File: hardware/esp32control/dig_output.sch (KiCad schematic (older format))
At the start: 6 parts, among them Q1 BSS138, U2 AQY212

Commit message: pcb update
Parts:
- R1: value 10k -> 1k
- R2: value 470 -> 1k
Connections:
- net VDD: now also U2.1; no longer R1.2
- net nIn: no longer U2.2
- net at R1.1: now also Q1.3 (D), R2.2; no longer U2.1
- net at D1.1 (K): now also R2.1; no longer R2.2
- new net: R1.2, U2.2
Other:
- moved on the sheet: D11, Q4, R26, R27
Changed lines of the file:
@@
 $Descr A4 11693 8268
 encoding utf-8
-Sheet 2 5
+Sheet 5 5
 Title ""
 Date ""
@@
 AR Path="/5C1F9DEA/5C1D222E" Ref="U6"  Part="1"
 AR Path="/5C1F9DF5/5C1D222E" Ref="U7"  Part="1"
-F 0 "U2" H 5300 3215 50  0000 C CNN
+F 0 "U7" H 5300 3215 50  0000 C CNN
 F 1 "AQY212" H 5300 3124 50  0000 C CNN
 F 2 "Housings_DIP:DIP-4_W7.62mm_SMDSocket_SmallPads" H 5300 3033 50  0000 C CIN
@@
 	1    0    0    -1
 $EndComp
-Wire Wire Line
-	5000 2900 4250 2900
 Text Label 4650 2900 0    60   ~ 0
 CH1
@@
 L esp32control-rescue:R-device-esp32ValveControl-rescue R1
 U 1 1 5C1D2239
-P 4850 2700
+P 4750 3350
 AR Path="/5C171864/5C1D2239" Ref="R1"  Part="1"
 AR Path="/5C171864/5C1D0CB5/5C1D2239" Ref="R?"  Part="1"
@@
 AR Path="/5C1F9DF5/5C1D2239" Ref="R26"  Part="1"
 AR Path="/5C1D2239" Ref="R26"  Part="1"
-F 0 "R1" V 4930 2700 50  0000 C CNN
-F 1 "10k" V 4850 2700 50  0000 C CNN
-F 2 "Resistors_SMD:R_0603" V 4780 2700 30  0001 C CNN
-F 3 "" H 4850 2700 30  0000 C CNN
-	1    4850 2700
-	0    1    -1   0
+F 0 "R26" V 4830 3350 50  0000 C CNN
+F 1 "1k" V 4750 3350 50  0000 C CNN
+F 2 "Resistors_SMD:R_0603" V 4680 3350 30  0001 C CNN
+F 3 "" H 4750 3350 30  0000 C CNN
+	1    4750 3350
+	1    0    0    1
 $EndComp
 Text HLabel 4150 2900 0    60   Input ~ 0
@@
 Text HLabel 6200 2900 2    60   Output ~ 0
 Out
-Wire Wire Line
-	4700 2700 4350 2700
 Text HLabel 6000 2700 2    60   Input ~ 0
 Vin
@@
 AR Path="/5C1F9DEA/5C1D2245" Ref="D10"  Part="1"
 AR Path="/5C1F9DF5/5C1D2245" Ref="D12"  Part="1"
-F 0 "D2" H 6000 3350 50  0000 C CNN
+F 0 "D12" H 6000 3350 50  0000 C CNN
 F 1 "TVS" H 6000 3050 50  0000 C CNN
 F 2 "Diodes_SMD:D_SMA" H 6000 3200 60  0001 C CNN
@@
 Wire Wire Line
 	6000 2900 6200 2900
-Text HLabel 6200 3800 2    60   Input ~ 0
+Text HLabel 6200 3900 2    60   Input ~ 0
 GND
 $Comp
 L esp32control-rescue:LED-device-esp32ValveControl-rescue D?
 U 1 1 5C1D2251
-P 4750 3500
+P 4500 2950
 AR Path="/5C1D2251" Ref="D?"  Part="1"
 AR Path="/5C171864/5C1D2251" Ref="D1"  Part="1"
@@
 AR Path="/5C1F9DEA/5C1D2251" Ref="D9"  Part="1"
 AR Path="/5C1F9DF5/5C1D2251" Ref="D11"  Part="1"
-F 0 "D1" H 4750 3600 50  0000 C CNN
-F 1 "LED" H 4750 3400 50  0000 C CNN
-F 2 "LEDs:LED_0603_HandSoldering" H 4750 3500 50  0001 C CNN
-F 3 "" H 4750 3500 50  0000 C CNN
-	1    4750 3500
-	-1   0    0    1
-$EndComp
-$Comp
-L transistors:BSS138 Q?
-U 1 1 5C1D2258
-P 5450 3600
-AR Path="/5C1D2258" Ref="Q?"  Part="1"
-AR Path="/5C171864/5C1D2258" Ref="Q1"  Part="1"
-AR Path="/5C1F3716/5C1D2258" Ref="Q2"  Part="1"
-AR Path="/5C1F9DEA/5C1D2258" Ref="Q3"  Part="1"
-AR Path="/5C1F9DF5/5C1D2258" Ref="Q4"  Part="1"
-F 0 "Q1" H 5450 3451 40  0000 R CNN
-F 1 "BSS138" H 5450 3750 40  0000 R CNN
-F 2 "Package_TO_SOT_SMD:SOT-23" H 5320 3702 29  0000 C CNN
-F 3 "" H 5450 3600 60  0000 C CNN
-	1    5450 3600
+F 0 "D11" H 4500 3050 50  0000 C CNN
+F 1 "LED" H 4500 2850 50  0000 C CNN
+F 2 "LEDs:LED_0603_HandSoldering" H 4500 2950 50  0001 C CNN
+F 3 "" H 4500 2950 50  0000 C CNN
+	1    4500 2950
 	0    -1   -1   0
 $EndComp
@@
 L esp32control-rescue:R-device-esp32ValveControl-rescue R?
 U 1 1 5C1D225F
-P 5100 3500
+P 4500 3350
 AR Path="/5C1D225F" Ref="R?"  Part="1"
 AR Path="/5C171864/5C1D225F" Ref="R2"  Part="1"
@@
 AR Path="/5C1F9DEA/5C1D225F" Ref="R25"  Part="1"
 AR Path="/5C1F9DF5/5C1D225F" Ref="R27"  Part="1"
-F 0 "R2" V 5180 3500 50  0000 C CNN
-F 1 "470" V 5100 3500 50  0000 C CNN
-F 2 "Resistors_SMD:R_0603" V 5030 3500 30  0001 C CNN
-F 3 "" H 5100 3500 30  0000 C CNN
-	1    5100 3500
-	0    1    1    0
+F 0 "R27" V 4580 3350 50  0000 C CNN
+F 1 "1k" V 4500 3350 50  0000 C CNN
+F 2 "Resistors_SMD:R_0603" V 4430 3350 30  0001 C CNN
+F 3 "" H 4500 3350 30  0000 C CNN
+	1    4500 3350
+	1    0    0    -1
 $EndComp
 Wire Wire Line
-	4550 3500 4350 3500
-Wire Wire Line
-	4350 3500 4350 2700
-Connection ~ 4350 2700
-Wire Wire Line
-	4350 2700 4150 2700
-Wire Wire Line
-	5500 3800 4250 3800
-Wire Wire Line
-	4250 3800 4250 2900
-Connection ~ 4250 2900
+	4250 3750 4250 2900
 Wire Wire Line
 	4250 2900 4150 2900
-Wire Wire Line
-	5650 3800 5650 3500
 Text HLabel 6200 3550 2    50   Input ~ 0
 GNDA
@@
 	6000 3550 6000 3500
 Wire Wire Line
-	5650 3800 6200 3800
+	4300 3750 4250 3750
+$Comp
+L transistors:BSS138 Q?
+U 1 1 5C1D2258
+P 4500 3700
+AR Path="/5C1D2258" Ref="Q?"  Part="1"
+AR Path="/5C171864/5C1D2258" Ref="Q1"  Part="1"
+AR Path="/5C1F3716/5C1D2258" Ref="Q2"  Part="1"
+AR Path="/5C1F9DEA/5C1D2258" Ref="Q3"  Part="1"
+AR Path="/5C1F9DF5/5C1D2258" Ref="Q4"  Part="1"
+F 0 "Q4" H 4500 3551 40  0000 R CNN
+F 1 "BSS138" H 4500 3850 40  0000 R CNN
+F 2 "Package_TO_SOT_SMD:SOT-23" H 4370 3802 29  0000 C CNN
+F 3 "" H 4500 3700 60  0000 C CNN
+	1    4500 3700
+	1    0    0    -1
+$EndComp
+Wire Wire Line
+	5000 2900 4750 2900
+Wire Wire Line
+	4150 2700 4500 2700
+Wire Wire Line
+	4500 2750 4500 2700
+Connection ~ 4500 2700
+Wire Wire Line
+	4500 3150 4500 3200
+Wire Wire Line
+	4500 3500 4600 3500
+Wire Wire Line
+	4750 3200 4750 2900
+Wire Wire Line
+	4500 2700 5000 2700
+Connection ~ 4600 3500
+Wire Wire Line
+	4600 3500 4750 3500
+Wire Wire Line
+	4600 3900 6200 3900
 $EndSCHEMATC

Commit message: update libs to kicad 5.1.5
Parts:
- D2: footprint Diodes_SMD:D_SMA -> Diode_SMD:D_SMA
- R1, R2: footprint Resistors_SMD:R_0603 -> Resistor_SMD:R_0603_1608Metric; symbol esp32control-rescue:R-device-esp32ValveControl-rescue -> Device:R
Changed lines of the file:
@@
 EESchema Schematic File Version 4
-LIBS:esp32control-cache
-EELAYER 26 0
+EELAYER 30 0
 EELAYER END
 $Descr A4 11693 8268
 encoding utf-8
-Sheet 5 5
+Sheet 2 5
 Title ""
 Date ""
@@
 AR Path="/5C1F9DEA/5C1D222E" Ref="U6"  Part="1"
 AR Path="/5C1F9DF5/5C1D222E" Ref="U7"  Part="1"
-F 0 "U7" H 5300 3215 50  0000 C CNN
+F 0 "U2" H 5300 3215 50  0000 C CNN
 F 1 "AQY212" H 5300 3124 50  0000 C CNN
 F 2 "Housings_DIP:DIP-4_W7.62mm_SMDSocket_SmallPads" H 5300 3033 50  0000 C CIN
@@
 Vin
 $Comp
-L esp32control-rescue:R-device-esp32ValveControl-rescue R1
+L Device:R R1
 U 1 1 5C1D2239
 P 4750 3350
@@
 AR Path="/5C1F9DF5/5C1D2239" Ref="R26"  Part="1"
 AR Path="/5C1D2239" Ref="R26"  Part="1"
-F 0 "R26" V 4830 3350 50  0000 C CNN
+F 0 "R1" V 4830 3350 50  0000 C CNN
 F 1 "1k" V 4750 3350 50  0000 C CNN
-F 2 "Resistors_SMD:R_0603" V 4680 3350 30  0001 C CNN
+F 2 "Resistor_SMD:R_0603_1608Metric" V 4680 3350 30  0001 C CNN
 F 3 "" H 4750 3350 30  0000 C CNN
 	1    4750 3350
@@
 AR Path="/5C1F9DEA/5C1D2245" Ref="D10"  Part="1"
 AR Path="/5C1F9DF5/5C1D2245" Ref="D12"  Part="1"
-F 0 "D12" H 6000 3350 50  0000 C CNN
+F 0 "D2" H 6000 3350 50  0000 C CNN
 F 1 "TVS" H 6000 3050 50  0000 C CNN
-F 2 "Diodes_SMD:D_SMA" H 6000 3200 60  0001 C CNN
+F 2 "Diode_SMD:D_SMA" H 6000 3200 60  0001 C CNN
 F 3 "" H 6000 3200 60  0000 C CNN
 	1    6000 3200
@@
 AR Path="/5C1F9DEA/5C1D2251" Ref="D9"  Part="1"
 AR Path="/5C1F9DF5/5C1D2251" Ref="D11"  Part="1"
-F 0 "D11" H 4500 3050 50  0000 C CNN
+F 0 "D1" H 4500 3050 50  0000 C CNN
 F 1 "LED" H 4500 2850 50  0000 C CNN
 F 2 "LEDs:LED_0603_HandSoldering" H 4500 2950 50  0001 C CNN
@@
 $EndComp
 $Comp
-L esp32control-rescue:R-device-esp32ValveControl-rescue R?
+L Device:R R?
 U 1 1 5C1D225F
 P 4500 3350
@@
 AR Path="/5C1F9DEA/5C1D225F" Ref="R25"  Part="1"
 AR Path="/5C1F9DF5/5C1D225F" Ref="R27"  Part="1"
-F 0 "R27" V 4580 3350 50  0000 C CNN
+F 0 "R2" V 4580 3350 50  0000 C CNN
 F 1 "1k" V 4500 3350 50  0000 C CNN
-F 2 "Resistors_SMD:R_0603" V 4430 3350 30  0001 C CNN
+F 2 "Resistor_SMD:R_0603_1608Metric" V 4430 3350 30  0001 C CNN
 F 3 "" H 4500 3350 30  0000 C CNN
 	1    4500 3350
@@
 AR Path="/5C1F9DEA/5C1D2258" Ref="Q3"  Part="1"
 AR Path="/5C1F9DF5/5C1D2258" Ref="Q4"  Part="1"
-F 0 "Q4" H 4500 3551 40  0000 R CNN
+F 0 "Q1" H 4500 3551 40  0000 R CNN
 F 1 "BSS138" H 4500 3850 40  0000 R CNN
 F 2 "Package_TO_SOT_SMD:SOT-23" H 4370 3802 29  0000 C CNN

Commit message: revB initial
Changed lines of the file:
@@
 AR Path="/5C1F9DEA/5C1D222E" Ref="U6"  Part="1"
 AR Path="/5C1F9DF5/5C1D222E" Ref="U7"  Part="1"
-F 0 "U2" H 5300 3215 50  0000 C CNN
+F 0 "U7" H 5300 3215 50  0000 C CNN
 F 1 "AQY212" H 5300 3124 50  0000 C CNN
 F 2 "Housings_DIP:DIP-4_W7.62mm_SMDSocket_SmallPads" H 5300 3033 50  0000 C CIN
@@
 AR Path="/5C1F9DF5/5C1D2239" Ref="R26"  Part="1"
 AR Path="/5C1D2239" Ref="R26"  Part="1"
-F 0 "R1" V 4830 3350 50  0000 C CNN
+F 0 "R26" V 4830 3350 50  0000 C CNN
 F 1 "1k" V 4750 3350 50  0000 C CNN
 F 2 "Resistor_SMD:R_0603_1608Metric" V 4680 3350 30  0001 C CNN
@@
 AR Path="/5C1F9DEA/5C1D2245" Ref="D10"  Part="1"
 AR Path="/5C1F9DF5/5C1D2245" Ref="D12"  Part="1"
-F 0 "D2" H 6000 3350 50  0000 C CNN
+F 0 "D12" H 6000 3350 50  0000 C CNN
 F 1 "TVS" H 6000 3050 50  0000 C CNN
 F 2 "Diode_SMD:D_SMA" H 6000 3200 60  0001 C CNN
@@
 AR Path="/5C1F9DEA/5C1D2251" Ref="D9"  Part="1"
 AR Path="/5C1F9DF5/5C1D2251" Ref="D11"  Part="1"
-F 0 "D1" H 4500 3050 50  0000 C CNN
+F 0 "D11" H 4500 3050 50  0000 C CNN
 F 1 "LED" H 4500 2850 50  0000 C CNN
 F 2 "LEDs:LED_0603_HandSoldering" H 4500 2950 50  0001 C CNN
@@
 AR Path="/5C1F9DEA/5C1D225F" Ref="R25"  Part="1"
 AR Path="/5C1F9DF5/5C1D225F" Ref="R27"  Part="1"
-F 0 "R2" V 4580 3350 50  0000 C CNN
+F 0 "R27" V 4580 3350 50  0000 C CNN
 F 1 "1k" V 4500 3350 50  0000 C CNN
 F 2 "Resistor_SMD:R_0603_1608Metric" V 4430 3350 30  0001 C CNN
@@
 AR Path="/5C1F9DEA/5C1D2258" Ref="Q3"  Part="1"
 AR Path="/5C1F9DF5/5C1D2258" Ref="Q4"  Part="1"
-F 0 "Q1" H 4500 3551 40  0000 R CNN
+F 0 "Q4" H 4500 3551 40  0000 R CNN
 F 1 "BSS138" H 4500 3850 40  0000 R CNN
 F 2 "Package_TO_SOT_SMD:SOT-23" H 4370 3802 29  0000 C CNN

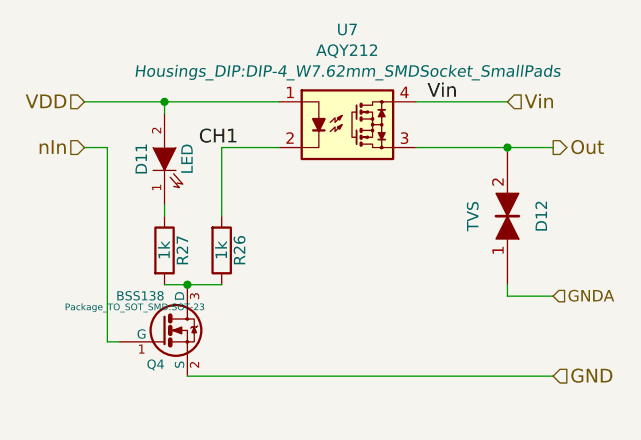
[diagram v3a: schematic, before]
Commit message: switched position of con and esp in layout
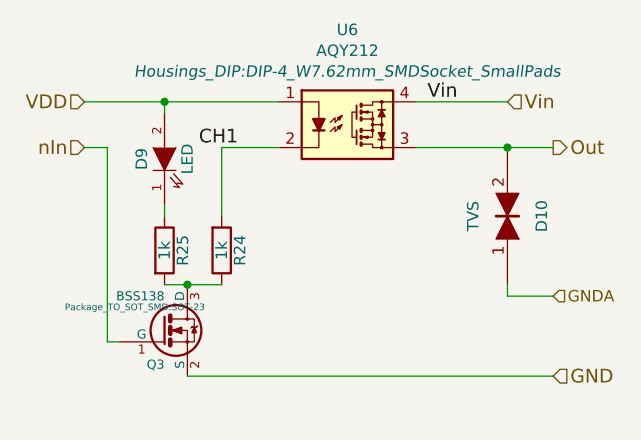
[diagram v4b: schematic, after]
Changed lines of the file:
@@
 $Descr A4 11693 8268
 encoding utf-8
-Sheet 2 5
+Sheet 4 5
 Title ""
 Date ""
@@
 AR Path="/5C1F9DEA/5C1D222E" Ref="U6"  Part="1"
 AR Path="/5C1F9DF5/5C1D222E" Ref="U7"  Part="1"
-F 0 "U7" H 5300 3215 50  0000 C CNN
+F 0 "U6" H 5300 3215 50  0000 C CNN
 F 1 "AQY212" H 5300 3124 50  0000 C CNN
 F 2 "Housings_DIP:DIP-4_W7.62mm_SMDSocket_SmallPads" H 5300 3033 50  0000 C CIN
@@
 AR Path="/5C1F9DF5/5C1D2239" Ref="R26"  Part="1"
 AR Path="/5C1D2239" Ref="R26"  Part="1"
-F 0 "R26" V 4830 3350 50  0000 C CNN
+F 0 "R24" V 4830 3350 50  0000 C CNN
 F 1 "1k" V 4750 3350 50  0000 C CNN
 F 2 "Resistor_SMD:R_0603_1608Metric" V 4680 3350 30  0001 C CNN
@@
 AR Path="/5C1F9DEA/5C1D2245" Ref="D10"  Part="1"
 AR Path="/5C1F9DF5/5C1D2245" Ref="D12"  Part="1"
-F 0 "D12" H 6000 3350 50  0000 C CNN
+F 0 "D10" H 6000 3350 50  0000 C CNN
 F 1 "TVS" H 6000 3050 50  0000 C CNN
 F 2 "Diode_SMD:D_SMA" H 6000 3200 60  0001 C CNN
@@
 AR Path="/5C1F9DEA/5C1D2251" Ref="D9"  Part="1"
 AR Path="/5C1F9DF5/5C1D2251" Ref="D11"  Part="1"
-F 0 "D11" H 4500 3050 50  0000 C CNN
+F 0 "D9" H 4500 3050 50  0000 C CNN
 F 1 "LED" H 4500 2850 50  0000 C CNN
 F 2 "LEDs:LED_0603_HandSoldering" H 4500 2950 50  0001 C CNN
@@
 AR Path="/5C1F9DEA/5C1D225F" Ref="R25"  Part="1"
 AR Path="/5C1F9DF5/5C1D225F" Ref="R27"  Part="1"
-F 0 "R27" V 4580 3350 50  0000 C CNN
+F 0 "R25" V 4580 3350 50  0000 C CNN
 F 1 "1k" V 4500 3350 50  0000 C CNN
 F 2 "Resistor_SMD:R_0603_1608Metric" V 4430 3350 30  0001 C CNN
@@
 AR Path="/5C1F9DEA/5C1D2258" Ref="Q3"  Part="1"
 AR Path="/5C1F9DF5/5C1D2258" Ref="Q4"  Part="1"
-F 0 "Q4" H 4500 3551 40  0000 R CNN
+F 0 "Q3" H 4500 3551 40  0000 R CNN
 F 1 "BSS138" H 4500 3850 40  0000 R CNN
 F 2 "Package_TO_SOT_SMD:SOT-23" H 4370 3802 29  0000 C CNN

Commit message: bom update
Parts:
- D2: value TVS -> SMAJ26CAQ; Mouser (none) -> 621-SMAJ26CAQ-13-F
- Q1: Mouser (none) -> 771-BSS138P215
- U2: Mouser (none) -> 769-AQY212GS
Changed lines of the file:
@@
 F 2 "Housings_DIP:DIP-4_W7.62mm_SMDSocket_SmallPads" H 5300 3033 50  0000 C CIN
 F 3 "http://www.semicon.toshiba.co.jp/docs/datasheet/en/Opto/TLP222A_TLP222A-2_en_datasheet_071001.pdf" H 5300 3034 50  0001 C CNN
+F 4 " 769-AQY212GS " H 5300 2800 50  0001 C CNN "Mouser"
 	1    5300 2800
 	1    0    0    -1
@@
 AR Path="/5C1F9DF5/5C1D2245" Ref="D12"  Part="1"
 F 0 "D10" H 6000 3350 50  0000 C CNN
-F 1 "TVS" H 6000 3050 50  0000 C CNN
+F 1 "SMAJ26CAQ" H 6000 3050 50  0000 C CNN
 F 2 "Diode_SMD:D_SMA" H 6000 3200 60  0001 C CNN
 F 3 "" H 6000 3200 60  0000 C CNN
+F 4 " 621-SMAJ26CAQ-13-F " H 6000 3200 50  0001 C CNN "Mouser"
 	1    6000 3200
 	0    1    -1   0
@@
 F 2 "Package_TO_SOT_SMD:SOT-23" H 4370 3802 29  0000 C CNN
 F 3 "" H 4500 3700 60  0000 C CNN
+F 4 " 771-BSS138P215 " H 4500 3700 50  0001 C CNN "Mouser"
 	1    4500 3700
 	1    0    0    -1

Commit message: kicad6 update
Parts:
- D1: value LED -> yellow; Mouser (none) -> 710-150060YS75000
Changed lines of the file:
@@
 $Descr A4 11693 8268
 encoding utf-8
-Sheet 4 5
+Sheet 2 5
 Title ""
 Date ""
@@
 AR Path="/5C1F9DEA/5C1D222E" Ref="U6"  Part="1"
 AR Path="/5C1F9DF5/5C1D222E" Ref="U7"  Part="1"
-F 0 "U6" H 5300 3215 50  0000 C CNN
+F 0 "U2" H 5300 3215 50  0000 C CNN
 F 1 "AQY212" H 5300 3124 50  0000 C CNN
 F 2 "Housings_DIP:DIP-4_W7.62mm_SMDSocket_SmallPads" H 5300 3033 50  0000 C CIN
@@
 AR Path="/5C1F9DF5/5C1D2239" Ref="R26"  Part="1"
 AR Path="/5C1D2239" Ref="R26"  Part="1"
-F 0 "R24" V 4830 3350 50  0000 C CNN
+F 0 "R1" V 4830 3350 50  0000 C CNN
 F 1 "1k" V 4750 3350 50  0000 C CNN
 F 2 "Resistor_SMD:R_0603_1608Metric" V 4680 3350 30  0001 C CNN
@@
 AR Path="/5C1F9DEA/5C1D2245" Ref="D10"  Part="1"
 AR Path="/5C1F9DF5/5C1D2245" Ref="D12"  Part="1"
-F 0 "D10" H 6000 3350 50  0000 C CNN
+F 0 "D2" H 6000 3350 50  0000 C CNN
 F 1 "SMAJ26CAQ" H 6000 3050 50  0000 C CNN
 F 2 "Diode_SMD:D_SMA" H 6000 3200 60  0001 C CNN
@@
 AR Path="/5C1F9DEA/5C1D2251" Ref="D9"  Part="1"
 AR Path="/5C1F9DF5/5C1D2251" Ref="D11"  Part="1"
-F 0 "D9" H 4500 3050 50  0000 C CNN
-F 1 "LED" H 4500 2850 50  0000 C CNN
+F 0 "D1" H 4500 3050 50  0000 C CNN
+F 1 "yellow" H 4500 2850 50  0000 C CNN
 F 2 "LEDs:LED_0603_HandSoldering" H 4500 2950 50  0001 C CNN
 F 3 "" H 4500 2950 50  0000 C CNN
+F 4 " 710-150060YS75000 " H 4500 2950 50  0001 C CNN "Mouser"
 	1    4500 2950
 	0    -1   -1   0
@@
 AR Path="/5C1F9DEA/5C1D225F" Ref="R25"  Part="1"
 AR Path="/5C1F9DF5/5C1D225F" Ref="R27"  Part="1"
-F 0 "R25" V 4580 3350 50  0000 C CNN
+F 0 "R2" V 4580 3350 50  0000 C CNN
 F 1 "1k" V 4500 3350 50  0000 C CNN
 F 2 "Resistor_SMD:R_0603_1608Metric" V 4430 3350 30  0001 C CNN
@@
 AR Path="/5C1F9DEA/5C1D2258" Ref="Q3"  Part="1"
 AR Path="/5C1F9DF5/5C1D2258" Ref="Q4"  Part="1"
-F 0 "Q3" H 4500 3551 40  0000 R CNN
+F 0 "Q1" H 4500 3551 40  0000 R CNN
 F 1 "BSS138" H 4500 3850 40  0000 R CNN
 F 2 "Package_TO_SOT_SMD:SOT-23" H 4370 3802 29  0000 C CNN
